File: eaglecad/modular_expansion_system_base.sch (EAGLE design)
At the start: 36 parts, among them IC1 74LS244N, IC2 74LS244N, IC3 74LS244N, IC4 SRAM, IC5 74LS30N, IC6 74LS30N, IC7 7805T, IC8 74LS00N, IC9 7805T, J1_ADDRESS_CON j1, J2_DATA_AND_POWER_CON j2, J3 interrupt_wait_block, SW1 100SP3T1B1M6QE

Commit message: all three boards designed
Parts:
- removed C9: .1uf, rcl:C-US025-025X050
- removed IC5: 74LS30N, 74xx-us:74LS30N
- removed J3: interrupt_wait_block, SparkFun-Connectors:CONN_20
- removed RN1: 4.7k, resistor-dil:8R-N
- added J1-WAIT-AND-INT: WAIT-AND-INT, SparkFun-Connectors:CONN_04X2
- IC6: value 74LS30N -> 74LS20N; device 74xx-us:74LS30N -> 74xx-us:74LS20N
- RN2: device resistor-dil:8R-N -> resistor-sil:G08R
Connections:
- removed net INT*0: IC5A.I7, J3.1, RN2H.1
- removed net INT*1: IC5A.I6, J3.2, RN2G.1
- removed net INT*2: IC5A.I5, J3.3, RN2F.1
- removed net INT*3: IC5A.I4, J3.4, RN2E.1
- removed net INT*4: IC5A.I3, J3.5, RN2D.1
- removed net INT*5: IC5A.I2, J3.6, RN2C.1
- removed net INT*6: IC5A.I1, J3.7, RN2B.1
- removed net INT*7: IC5A.I0, J3.8, RN2A.1
- removed net N$21: IC6A.I2, J3.18, RN1C.1
- removed net WAIT*0: IC6A.I7, J3.13, RN1H.1
- removed net WAIT*1: IC6A.I6, J3.14, RN1G.1
- removed net WAIT*2: IC6A.I5, J3.15, RN1F.1
- removed net WAIT*3: IC6A.I4, J3.16, RN1E.1
- removed net WAIT*5: IC6A.I3, J3.17, RN1D.1
- removed net WAIT*6: IC6A.I1, J3.19, RN1B.1
- removed net WAIT*7: IC6A.I0, J3.20, RN1A.1
- new net INT0*: IC6A.I3, J1-WAIT-AND-INT.1, RN2.2
- new net INT1*: IC6A.I2, J1-WAIT-AND-INT.3, RN2.3
- new net INT2*: IC6A.I1, J1-WAIT-AND-INT.5, RN2.4
- new net INT3*: IC6A.I0, J1-WAIT-AND-INT.7, RN2.5
- new net WAIT0*: IC6B.I3, J1-WAIT-AND-INT.2, RN2.6
- new net WAIT1*: IC6B.I2, J1-WAIT-AND-INT.4, RN2.7
- new net WAIT2*: IC6B.I1, J1-WAIT-AND-INT.6, RN2.8
- new net WAIT3*: IC6B.I0, J1-WAIT-AND-INT.8, RN2.9
- net GND: now also IC6P.GND; no longer C9.2, IC5P.GND
- net INT: now also IC6A.O; no longer IC5A.O
- net VCC: now also IC6P.VCC, RN2.1; no longer C9.1, IC5P.VCC, RN1A.2, RN1B.2, RN1C.2, RN1D.2, RN1E.2, RN1F.2, RN1G.2, RN1H.2, RN2A.2, RN2B.2, RN2C.2, RN2D.2, RN2E.2, RN2F.2, RN2G.2, RN2H.2
- net WAIT: now also IC6B.O; no longer IC6A.O

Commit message: removed soft reset for vdp, added 12 voice sound
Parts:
- removed IC6: 74LS20N, 74xx-us:74LS20N
- removed J1-WAIT-AND-INT: WAIT-AND-INT, SparkFun-Connectors:CONN_04X2
- added IC10, IC5: 74LS30N, 74xx-us:74LS30N
- added J1-INTERRUPTS: INTERRUPTS, SparkFun-Connectors:CONN_04X2
- added J2-WAITS: WAITS, SparkFun-Connectors:CONN_04X2
- added RN1: 4.7k, resistor-sil:G08R
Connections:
- new net INT4*: IC5A.I0, J1-INTERRUPTS.2, RN2.9
- new net INT5*: IC5A.I1, J1-INTERRUPTS.4, RN2.8
- new net INT6*: IC5A.I2, J1-INTERRUPTS.6, RN2.7
- new net INT7*: IC5A.I3, J1-INTERRUPTS.8, RN2.6
- new net WAIT4*: IC10A.I4, J2-WAITS.7, RN1.5
- new net WAIT5*: IC10A.I5, J2-WAITS.5, RN1.4
- new net WAIT6*: IC10A.I6, J2-WAITS.3, RN1.3
- new net WAIT7*: IC10A.I7, J2-WAITS.1, RN1.2
- net GND: now also IC10P.GND, IC5P.GND; no longer IC6P.GND
- net INT: now also IC5A.O; no longer IC6A.O
- net INT0*: now also IC5A.I7, J1-INTERRUPTS.1; no longer IC6A.I3, J1-WAIT-AND-INT.1
- net INT1*: now also IC5A.I6, J1-INTERRUPTS.3; no longer IC6A.I2, J1-WAIT-AND-INT.3
- net INT2*: now also IC5A.I5, J1-INTERRUPTS.5; no longer IC6A.I1, J1-WAIT-AND-INT.5
- net INT3*: now also IC5A.I4, J1-INTERRUPTS.7; no longer IC6A.I0, J1-WAIT-AND-INT.7
- net VCC: now also IC10P.VCC, IC5P.VCC, RN1.1; no longer IC6P.VCC
- net WAIT: now also IC10A.O; no longer IC6B.O
- net WAIT0*: now also IC10A.I3, J2-WAITS.8, RN1.6; no longer IC6B.I3, J1-WAIT-AND-INT.2, RN2.6
- net WAIT1*: now also IC10A.I2, J2-WAITS.6, RN1.7; no longer IC6B.I2, J1-WAIT-AND-INT.4, RN2.7
- net WAIT2*: now also IC10A.I1, J2-WAITS.4, RN1.8; no longer IC6B.I1, J1-WAIT-AND-INT.6, RN2.8
- net WAIT3*: now also IC10A.I0, J2-WAITS.2, RN1.9; no longer IC6B.I0, J1-WAIT-AND-INT.8, RN2.9
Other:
- moved on the sheet: RN2

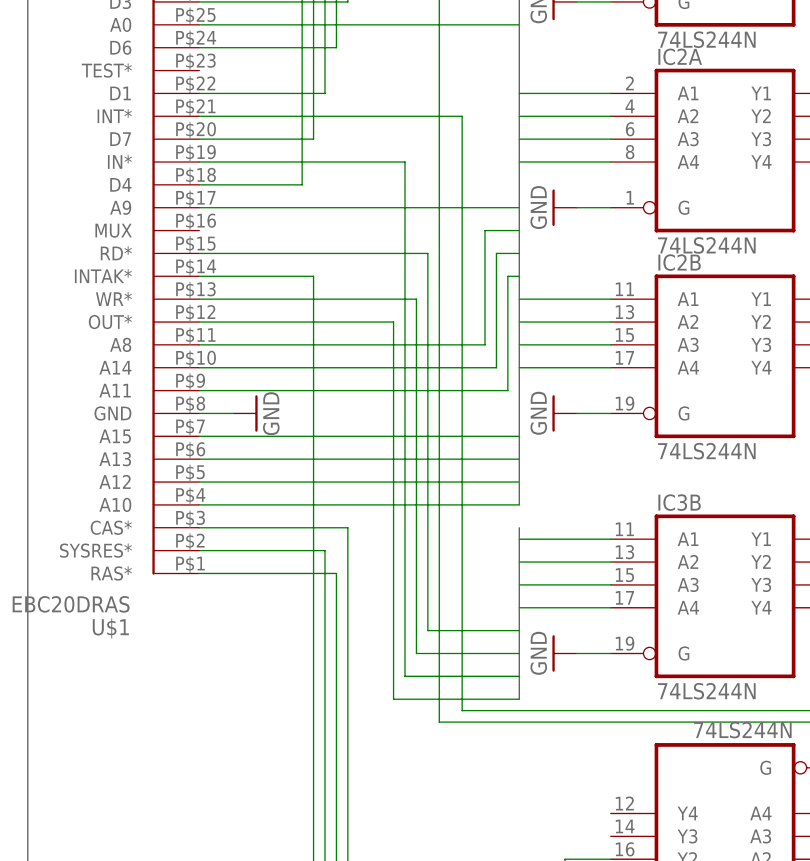
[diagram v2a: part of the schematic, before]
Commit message: bug in the base board RD, WR, IN, and OUT signals
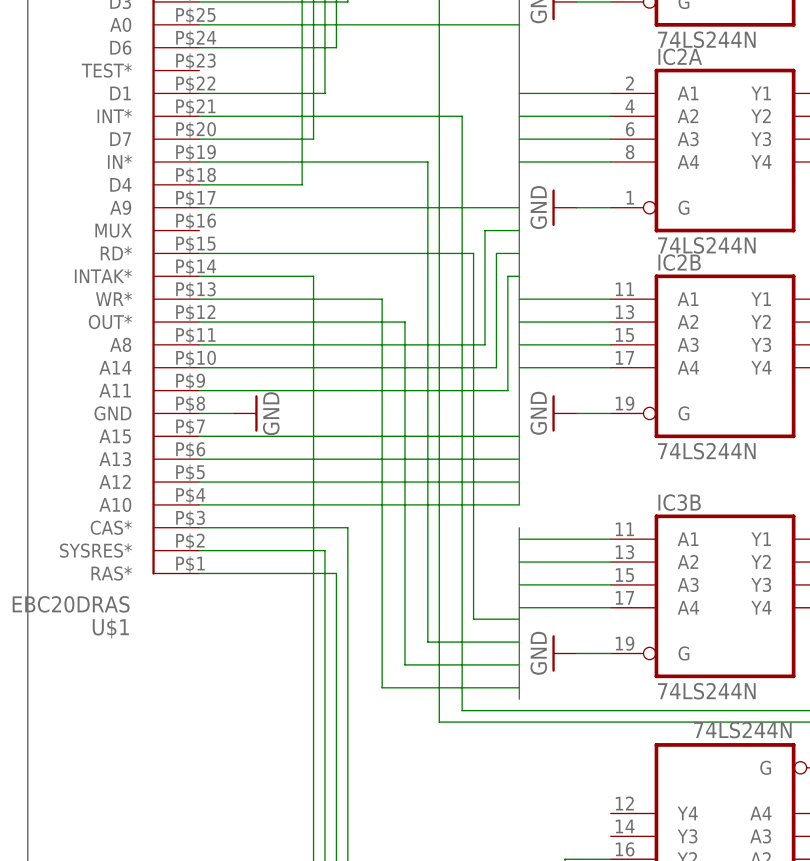
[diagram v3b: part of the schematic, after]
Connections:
- new net IN*: IC3B.A3, U$1.IN*
- new net OUT*: IC3B.A4, U$1.OUT*
- new net RD*: IC3B.A1, U$1.RD*
- new net WR*: IC3B.A2, U$1.WR*
- net BUFFERED_IN*: no longer IC3B.A3, U$1.IN*
- net BUFFERED_OUT*: no longer IC3B.A4, U$1.OUT*
- net BUFFERED_RD*: no longer IC3B.A1, U$1.RD*
- net BUFFERED_WR*: no longer IC3B.A2, U$1.WR*
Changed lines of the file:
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@@
 </segment>
 </bus>
-<bus name="CNTRL:BUFFERED_IN*,BUFFERED_OUT*,BUFFERED_RD*,BUFFERED_WR*">
+<bus name="CNTRL:IN*,OUT*,RD*,WR*">
 <segment>
 <wire x1="175.26" y1="71.12" x2="175.26" y2="52.07" width="0.762" layer="92"/>
@@
 <net name="BUFFERED_RD*" class="0">
 <segment>
-<wire x1="175.26" y1="59.69" x2="165.1" y2="59.69" width="0.1524" layer="91"/>
-<wire x1="165.1" y1="59.69" x2="165.1" y2="101.6" width="0.1524" layer="91"/>
-<pinref part="U$1" gate="G$1" pin="RD*"/>
-<wire x1="165.1" y1="101.6" x2="139.7" y2="101.6" width="0.1524" layer="91"/>
-</segment>
-<segment>
-<pinref part="IC3" gate="B" pin="A1"/>
-<wire x1="185.42" y1="69.85" x2="175.26" y2="69.85" width="0.1524" layer="91"/>
-</segment>
-<segment>
 <pinref part="IC3" gate="B" pin="Y1"/>
 <wire x1="218.44" y1="69.85" x2="210.82" y2="69.85" width="0.1524" layer="91"/>
@@
 <net name="BUFFERED_WR*" class="0">
 <segment>
-<wire x1="175.26" y1="57.15" x2="163.83" y2="57.15" width="0.1524" layer="91"/>
-<wire x1="163.83" y1="57.15" x2="163.83" y2="96.52" width="0.1524" layer="91"/>
-<pinref part="U$1" gate="G$1" pin="WR*"/>
-<wire x1="163.83" y1="96.52" x2="139.7" y2="96.52" width="0.1524" layer="91"/>
-</segment>
-<segment>
-<pinref part="IC3" gate="B" pin="A2"/>
-<wire x1="175.26" y1="67.31" x2="185.42" y2="67.31" width="0.1524" layer="91"/>
-</segment>
-<segment>
 <pinref part="IC3" gate="B" pin="Y2"/>
 <wire x1="218.44" y1="67.31" x2="210.82" y2="67.31" width="0.1524" layer="91"/>
@@
 <net name="BUFFERED_IN*" class="0">
 <segment>
-<wire x1="175.26" y1="54.61" x2="162.56" y2="54.61" width="0.1524" layer="91"/>
-<wire x1="162.56" y1="54.61" x2="162.56" y2="111.76" width="0.1524" layer="91"/>
-<pinref part="U$1" gate="G$1" pin="IN*"/>
-<wire x1="162.56" y1="111.76" x2="139.7" y2="111.76" width="0.1524" layer="91"/>
-</segment>
-<segment>
-<pinref part="IC3" gate="B" pin="A3"/>
-<wire x1="175.26" y1="64.77" x2="185.42" y2="64.77" width="0.1524" layer="91"/>
-</segment>
-<segment>
 <pinref part="IC3" gate="B" pin="Y3"/>
 <wire x1="218.44" y1="64.77" x2="210.82" y2="64.77" width="0.1524" layer="91"/>
@@
 </net>
 <net name="BUFFERED_OUT*" class="0">
-<segment>
-<wire x1="175.26" y1="52.07" x2="161.29" y2="52.07" width="0.1524" layer="91"/>
-<wire x1="161.29" y1="52.07" x2="161.29" y2="93.98" width="0.1524" layer="91"/>
-<pinref part="U$1" gate="G$1" pin="OUT*"/>
-<wire x1="161.29" y1="93.98" x2="139.7" y2="93.98" width="0.1524" layer="91"/>
-</segment>
-<segment>
-<pinref part="IC3" gate="B" pin="A4"/>
-<wire x1="175.26" y1="62.23" x2="185.42" y2="62.23" width="0.1524" layer="91"/>
-</segment>
 <segment>
 <pinref part="IC3" gate="B" pin="Y4"/>
@@
 </segment>
 </net>
+<net name="RD*" class="0">
+<segment>
+<pinref part="U$1" gate="G$1" pin="RD*"/>
+<wire x1="139.7" y1="101.6" x2="170.18" y2="101.6" width="0.1524" layer="91"/>
+<wire x1="170.18" y1="101.6" x2="170.18" y2="60.96" width="0.1524" layer="91"/>
+<wire x1="170.18" y1="60.96" x2="175.26" y2="60.96" width="0.1524" layer="91"/>
+</segment>
+<segment>
+<pinref part="IC3" gate="B" pin="A1"/>
+<wire x1="175.26" y1="69.85" x2="185.42" y2="69.85" width="0.1524" layer="91"/>
+</segment>
+</net>
+<net name="IN*" class="0">
+<segment>
+<pinref part="U$1" gate="G$1" pin="IN*"/>
+<wire x1="139.7" y1="111.76" x2="165.1" y2="111.76" width="0.1524" layer="91"/>
+<wire x1="165.1" y1="111.76" x2="165.1" y2="58.42" width="0.1524" layer="91"/>
+<wire x1="165.1" y1="58.42" x2="175.26" y2="58.42" width="0.1524" layer="91"/>
+</segment>
+<segment>
+<pinref part="IC3" gate="B" pin="A3"/>
+<wire x1="175.26" y1="64.77" x2="185.42" y2="64.77" width="0.1524" layer="91"/>
+</segment>
+</net>
+<net name="OUT*" class="0">
+<segment>
+<pinref part="U$1" gate="G$1" pin="OUT*"/>
+<wire x1="139.7" y1="93.98" x2="162.56" y2="93.98" width="0.1524" layer="91"/>
+<wire x1="162.56" y1="93.98" x2="162.56" y2="55.88" width="0.1524" layer="91"/>
+<wire x1="162.56" y1="55.88" x2="175.26" y2="55.88" width="0.1524" layer="91"/>
+</segment>
+<segment>
+<pinref part="IC3" gate="B" pin="A4"/>
+<wire x1="175.26" y1="62.23" x2="185.42" y2="62.23" width="0.1524" layer="91"/>
+</segment>
+</net>
+<net name="WR*" class="0">
+<segment>
+<pinref part="U$1" gate="G$1" pin="WR*"/>
+<wire x1="139.7" y1="96.52" x2="160.02" y2="96.52" width="0.1524" layer="91"/>
+<wire x1="160.02" y1="96.52" x2="160.02" y2="53.34" width="0.1524" layer="91"/>
+<wire x1="160.02" y1="53.34" x2="175.26" y2="53.34" width="0.1524" layer="91"/>
+</segment>
+<segment>
+<pinref part="IC3" gate="B" pin="A2"/>
+<wire x1="175.26" y1="67.31" x2="185.42" y2="67.31" width="0.1524" layer="91"/>
+</segment>
+</net>

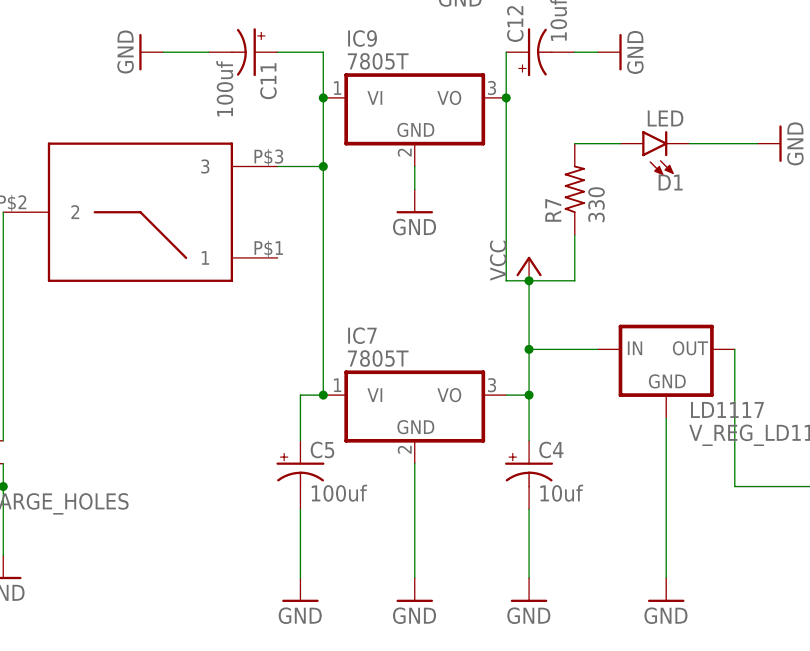
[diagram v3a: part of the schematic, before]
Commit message: added inductor to grfx brd and removed extra 7805
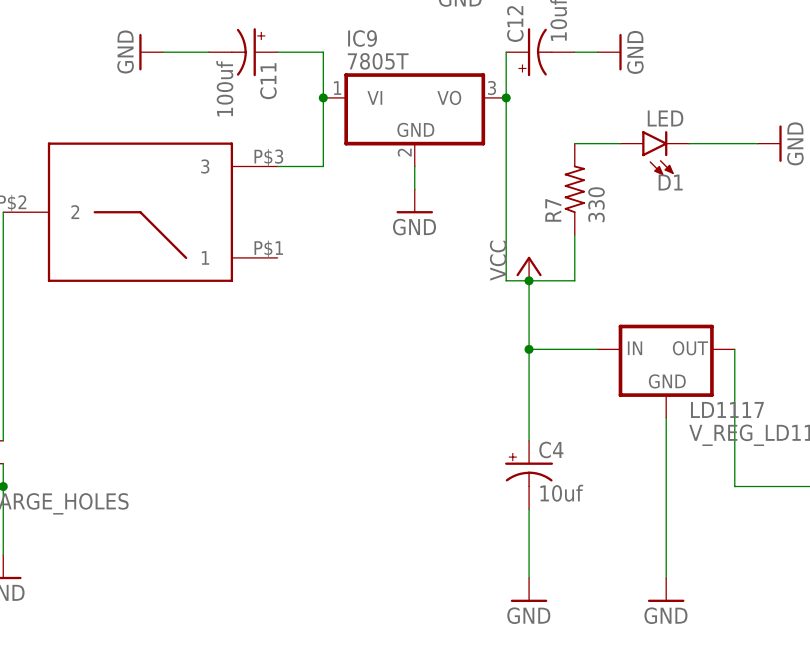
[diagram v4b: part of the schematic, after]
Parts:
- removed C5: 100uf, rcl:CPOL-USE2.5-5
- removed IC7: 7805T, linear:7805T
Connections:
- net GND: no longer C5.-, IC7.GND
- net VCC: no longer IC7.VO
- net VOLTAGE-IN: no longer C5.+, IC7.VI
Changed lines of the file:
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@@
 <setting verticaltext="up"/>
 </settings>
-<grid distance="0.05" unitdist="inch" unit="inch" style="lines" multiple="1" display="no" altdistance="0.005" altunitdist="inch" altunit="inch"/>
+<grid distance="0.1" unitdist="inch" unit="inch" style="lines" multiple="1" display="no" altdistance="0.01" altunitdist="inch" altunit="inch"/>
 <layers>
 <layer number="1" name="Top" color="4" fill="1" visible="no" active="no"/>
@@
 <part name="J1_ADDRESS_CON" library="SparkFun-Connectors" library_urn="urn:adsk.eagle:library:513" deviceset="CONN_20" device="" package3d_urn="urn:adsk.eagle:package:38196/1" value="j1"/>
 <part name="J2_DATA_AND_POWER_CON" library="SparkFun-Connectors" library_urn="urn:adsk.eagle:library:513" deviceset="CONN_20" device="" package3d_urn="urn:adsk.eagle:package:38196/1" value="j2"/>
-<part name="GND10" library="supply1" library_urn="urn:adsk.eagle:library:371" deviceset="GND" device=""/>
-<part name="GND11" library="supply1" library_urn="urn:adsk.eagle:library:371" deviceset="GND" device=""/>
 <part name="GND12" library="supply1" library_urn="urn:adsk.eagle:library:371" deviceset="GND" device=""/>
 <part name="GND13" library="supply1" library_urn="urn:adsk.eagle:library:371" deviceset="GND" device=""/>
@@
 <part name="H4" library="SparkFun-Hardware" library_urn="urn:adsk.eagle:library:519" deviceset="STANDOFF_ELECTRICAL" device="" package3d_urn="urn:adsk.eagle:package:38631/1"/>
 <part name="GND20" library="supply1" library_urn="urn:adsk.eagle:library:371" deviceset="GND" device=""/>
-<part name="IC7" library="linear" library_urn="urn:adsk.eagle:library:262" deviceset="78*" device="T" package3d_urn="urn:adsk.eagle:package:16414/1" technology="05"/>
 <part name="SW1" library="TMS99" deviceset="100SP3T1B1M6QE" device=""/>
 <part name="IC9" library="linear" library_urn="urn:adsk.eagle:library:262" deviceset="78*" device="T" package3d_urn="urn:adsk.eagle:package:16414/1" technology="05"/>
 <part name="GND21" library="supply1" library_urn="urn:adsk.eagle:library:371" deviceset="GND" device=""/>
-<part name="C5" library="rcl" library_urn="urn:adsk.eagle:library:334" deviceset="CPOL-US" device="E2.5-5" package3d_urn="urn:adsk.eagle:package:23344/1" value="100uf"/>
 <part name="C11" library="rcl" library_urn="urn:adsk.eagle:library:334" deviceset="CPOL-US" device="E2.5-5" package3d_urn="urn:adsk.eagle:package:23344/1" value="100uf"/>
 <part name="GND22" library="supply1" library_urn="urn:adsk.eagle:library:371" deviceset="GND" device=""/>
@@
 <attribute name="NAME" x="260.35" y="5.842" size="1.778" layer="95" font="vector" rot="R180"/>
 </instance>
-<instance part="GND10" gate="1" x="48.26" y="5.08" smashed="yes">
-<attribute name="VALUE" x="45.72" y="2.54" size="1.778" layer="96"/>
-</instance>
-<instance part="GND11" gate="1" x="60.96" y="5.08" smashed="yes">
-<attribute name="VALUE" x="58.42" y="2.54" size="1.778" layer="96"/>
-</instance>
 <instance part="GND12" gate="1" x="73.66" y="5.08" smashed="yes">
 <attribute name="VALUE" x="71.12" y="2.54" size="1.778" layer="96"/>
@@
 <instance part="GND20" gate="1" x="63.5" y="111.76" smashed="yes">
 <attribute name="VALUE" x="60.96" y="109.22" size="1.778" layer="96"/>
-</instance>
-<instance part="IC7" gate="A1" x="60.96" y="27.94" smashed="yes">
-<attribute name="NAME" x="53.34" y="33.655" size="1.778" layer="95"/>
-<attribute name="VALUE" x="53.34" y="31.115" size="1.778" layer="96"/>
 </instance>
 <instance part="SW1" gate="G$1" x="40.64" y="58.42" smashed="yes" rot="R180"/>
@@
 <instance part="GND21" gate="1" x="60.96" y="48.26" smashed="yes">
 <attribute name="VALUE" x="58.42" y="45.72" size="1.778" layer="96"/>
-</instance>
-<instance part="C5" gate="G$1" x="48.26" y="20.32" smashed="yes">
-<attribute name="NAME" x="49.276" y="20.955" size="1.778" layer="95"/>
-<attribute name="VALUE" x="49.276" y="16.129" size="1.778" layer="96"/>
 </instance>
 <instance part="C11" gate="G$1" x="43.18" y="66.04" smashed="yes" rot="R270">
@@
 <pinref part="U$1" gate="G$1" pin="GND3"/>
 <wire x1="143.51" y1="157.48" x2="139.7" y2="157.48" width="0.1524" layer="91"/>
-</segment>
-<segment>
-<pinref part="GND10" gate="1" pin="GND"/>
-<wire x1="48.26" y1="15.24" x2="48.26" y2="7.62" width="0.1524" layer="91"/>
-<pinref part="C5" gate="G$1" pin="-"/>
-</segment>
-<segment>
-<pinref part="GND11" gate="1" pin="GND"/>
-<wire x1="60.96" y1="20.32" x2="60.96" y2="7.62" width="0.1524" layer="91"/>
-<pinref part="IC7" gate="A1" pin="GND"/>
 </segment>
 <segment>
@@
 <pinref part="P+10" gate="VCC" pin="VCC"/>
 <wire x1="73.66" y1="40.64" x2="73.66" y2="33.02" width="0.1524" layer="91"/>
-<wire x1="73.66" y1="33.02" x2="73.66" y2="27.94" width="0.1524" layer="91"/>
 <junction x="73.66" y="40.64"/>
-<wire x1="73.66" y1="27.94" x2="73.66" y2="22.86" width="0.1524" layer="91"/>
+<wire x1="73.66" y1="33.02" x2="73.66" y2="22.86" width="0.1524" layer="91"/>
 <wire x1="78.74" y1="40.64" x2="73.66" y2="40.64" width="0.1524" layer="91"/>
 <pinref part="R7" gate="G$1" pin="1"/>
@@
 <wire x1="81.28" y1="33.02" x2="73.66" y2="33.02" width="0.1524" layer="91"/>
 <junction x="73.66" y="33.02"/>
-<pinref part="IC7" gate="A1" pin="VO"/>
-<wire x1="71.12" y1="27.94" x2="73.66" y2="27.94" width="0.1524" layer="91"/>
-<junction x="73.66" y="27.94"/>
 <pinref part="IC9" gate="A1" pin="VO"/>
 <wire x1="71.12" y1="60.96" x2="71.12" y2="40.64" width="0.1524" layer="91"/>
@@
 <net name="VOLTAGE-IN" class="0">
 <segment>
-<wire x1="48.26" y1="27.94" x2="48.26" y2="22.86" width="0.1524" layer="91"/>
-<pinref part="IC7" gate="A1" pin="VI"/>
-<wire x1="50.8" y1="27.94" x2="48.26" y2="27.94" width="0.1524" layer="91"/>
-<wire x1="50.8" y1="53.34" x2="50.8" y2="27.94" width="0.1524" layer="91"/>
-<junction x="50.8" y="27.94"/>
 <pinref part="SW1" gate="G$1" pin="3"/>
 <wire x1="45.72" y1="53.34" x2="50.8" y2="53.34" width="0.1524" layer="91"/>
 <pinref part="IC9" gate="A1" pin="VI"/>
 <wire x1="50.8" y1="60.96" x2="50.8" y2="53.34" width="0.1524" layer="91"/>
-<junction x="50.8" y="53.34"/>
-<pinref part="C5" gate="G$1" pin="+"/>
 <pinref part="C11" gate="G$1" pin="+"/>
 <wire x1="45.72" y1="66.04" x2="50.8" y2="66.04" width="0.1524" layer="91"/>
